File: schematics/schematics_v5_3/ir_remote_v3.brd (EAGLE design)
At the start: 77.9 x 40.5 mm, 27 parts, among them IC1 AP1117E50G, Q1 10MHz, T11 TASTER3301, T12 TASTER3301, T13 TASTER3301, T14 TASTER3301, T15 TASTER3301

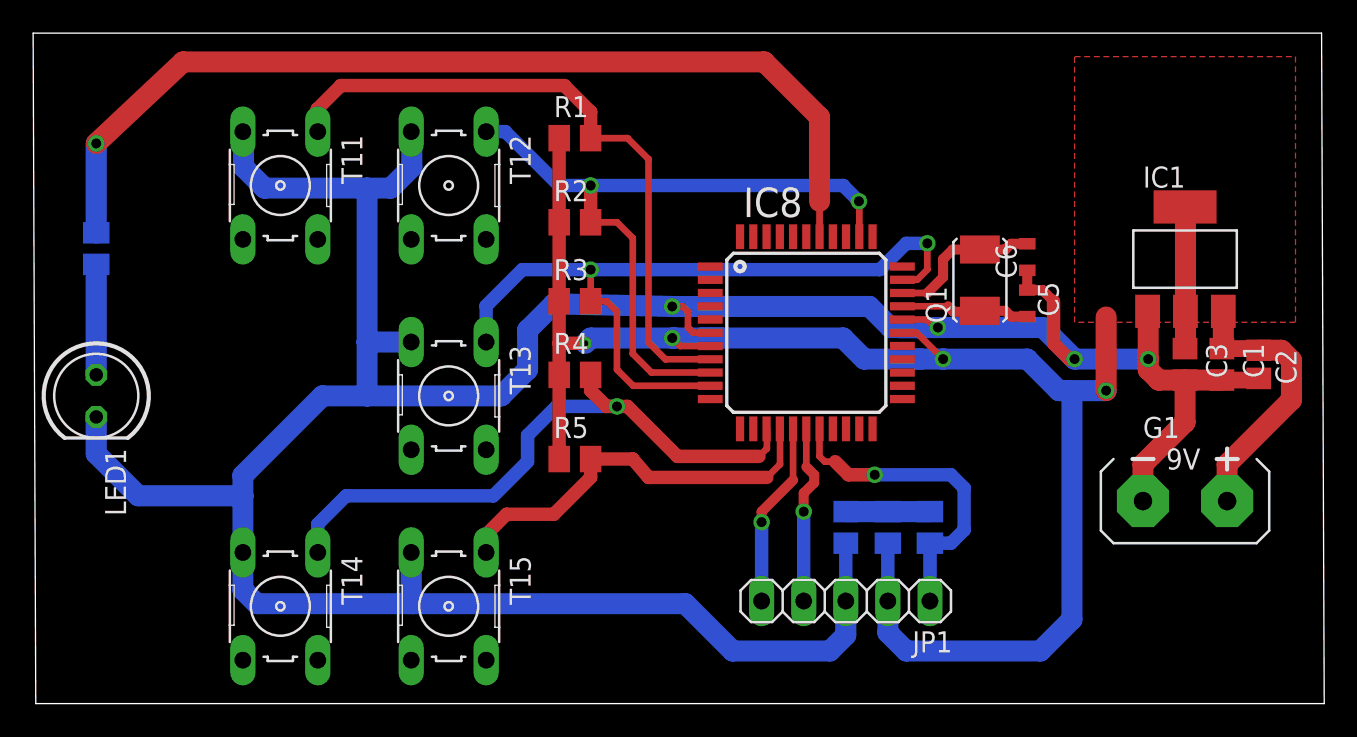
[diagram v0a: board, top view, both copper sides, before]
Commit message: Add minor modifications including ground and battery areas
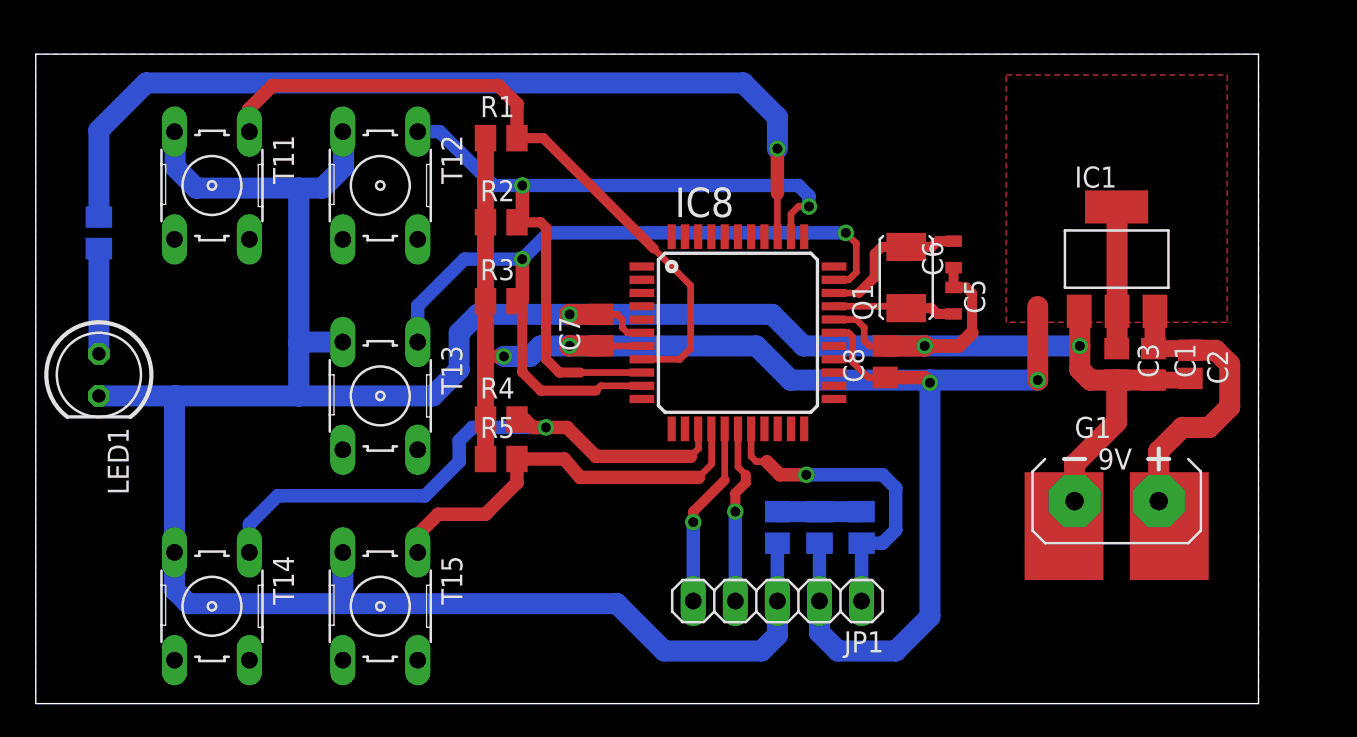
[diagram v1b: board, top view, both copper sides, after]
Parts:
- moved C7 6.68 mm to (34.1, 22.5), flipped to the top
- moved R4 5.20 mm to (28.1, 17.1)
- moved C5 4.45 mm to (55.4, 24.3)
- moved C6 4.45 mm to (55.4, 27.1)
- moved Q1 4.45 mm to (52.5, 25.7)
- moved R1 4.45 mm to (28.1, 34.1)
- moved R2 4.45 mm to (28.1, 29.1)
- moved R3 4.45 mm to (28.1, 24.3)
- moved R5 4.45 mm to (28.1, 14.8)
- moved C4 4.13 mm to (44.8, 10.6)
- moved IC8 4.13 mm to (42.4, 22.4)
- moved JP1 4.13 mm to (44.8, 6.19)
- moved R7 4.13 mm to (49.8, 10.6)
- moved R8 4.13 mm to (47.3, 10.6)
- moved T11 4.13 mm to (10.6, 31.3)
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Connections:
- removed net RDS_INT: IC8.36
- new net RC2: IC8.36, R6.1
- net RD0_LED: no longer R6.1
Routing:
- net RD0_LED: track 59.6 -> 0.00 mm, vias 1 -> 0
- net RC2: track 0.00 -> 55.5 mm, vias 0 -> 1
- net RB1: track 43.7 -> 46.9 mm
- net VCC: track 104.1 -> 106.8 mm
- net RB4: track 38.3 -> 36.0 mm
- net RB2: track 47.0 -> 49.1 mm
- net RB0: track 39.9 -> 41.9 mm
- net +9V: track 16.9 -> 18.3 mm
- net GND: track 190.4 -> 191.4 mm, vias 4 -> 3
- added copper zone on layer 16, net GND
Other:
- board size 77.9 x 40.5 mm -> 73.8 x 39.2 mm

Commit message: Add minor changes to layout v5_3
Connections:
- removed net RD0_LED: IC8.38
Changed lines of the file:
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@@
 <wire x1="30.63875" y1="34.13125" x2="37.30625" y2="27.46375" width="0.6096" layer="1"/>
-</signal>
-<signal name="RD0_LED">
-<contactref element="IC8" pad="38"/>
 </signal>
 <signal name="N$19">
